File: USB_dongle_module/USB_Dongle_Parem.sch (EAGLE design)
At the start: 29 parts, among them IC3 FT230XS, X1 USB-A

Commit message: Board
Board olemas, veidi vajab veel üle vaatamist, kuid oelemas siiski.
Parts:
- C7: device eagle-ltspice:CC0603 -> eagle-ltspice:CC1206
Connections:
- net TXD: now also R11.1
- net VCCIO: no longer R11.1
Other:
- moved on the sheet: C10, C7, R11, R12

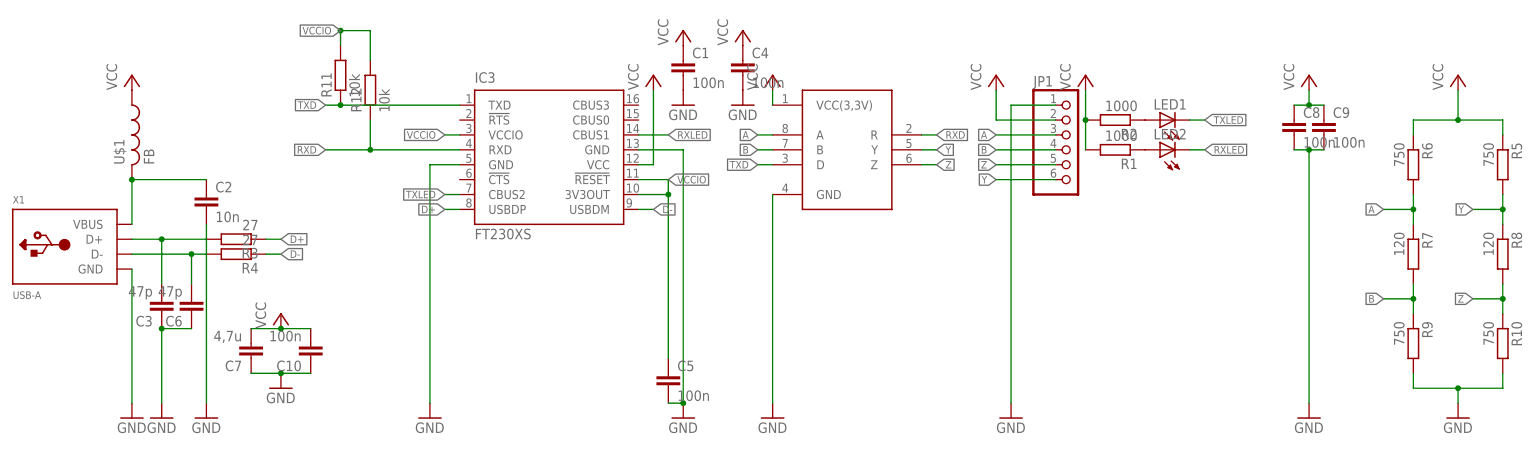
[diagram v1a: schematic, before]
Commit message: Korrastasin boardi
Tegin mõned muudatused skeemis ning korrastasin boardi. Valmis!
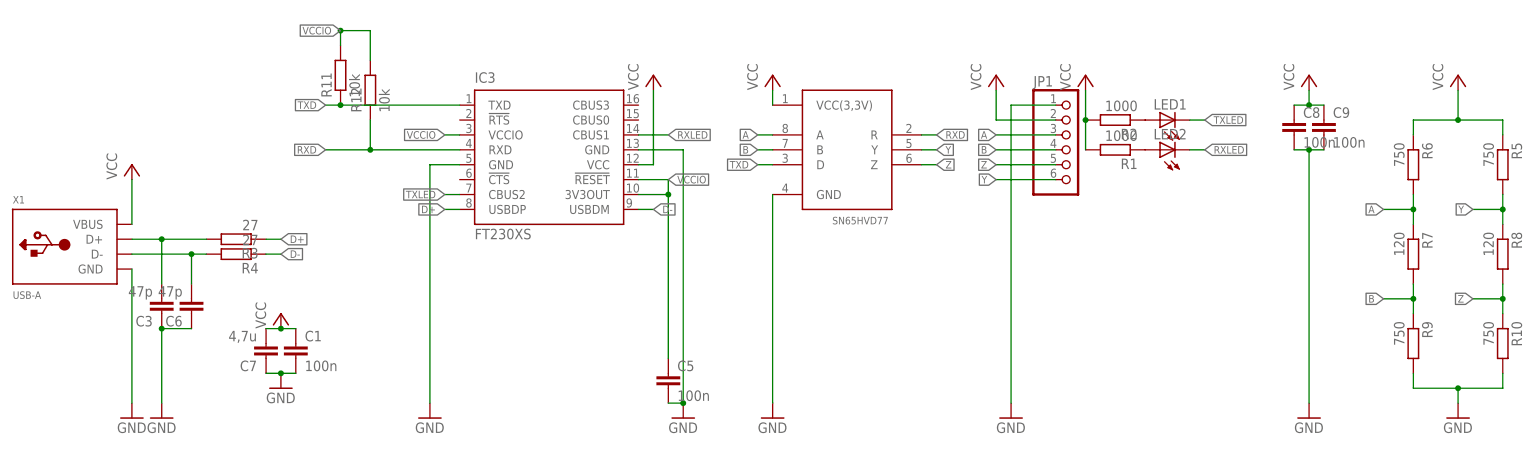
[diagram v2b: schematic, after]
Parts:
- removed C10, C4: 100n, eagle-ltspice:CC0603
- removed C2: 10n, eagle-ltspice:CC0603
- removed U$1: FB, adafruit:FB
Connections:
- removed net N$6: C2.1, U$1.2, X1.VBUS
- net GND: no longer C10.1, C2.2, C4.2
- net VCC: now also X1.VBUS; no longer C10.2, C4.1, U$1.1
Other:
- moved on the sheet: C1, C7

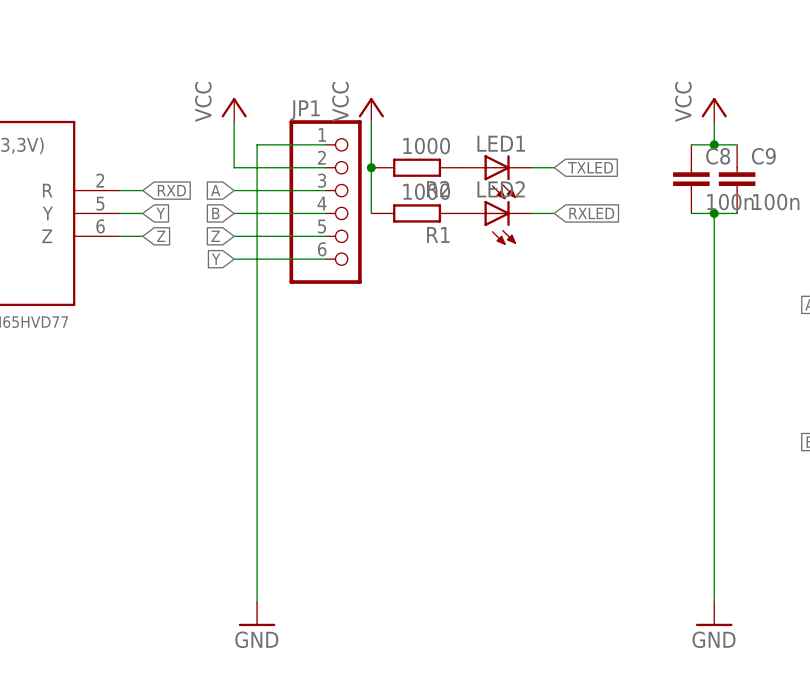
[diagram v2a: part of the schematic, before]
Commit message: Pinheader>Micromatch
Vahetasin siis komponendi välja, lisaks muutsin kondekate asukohta.
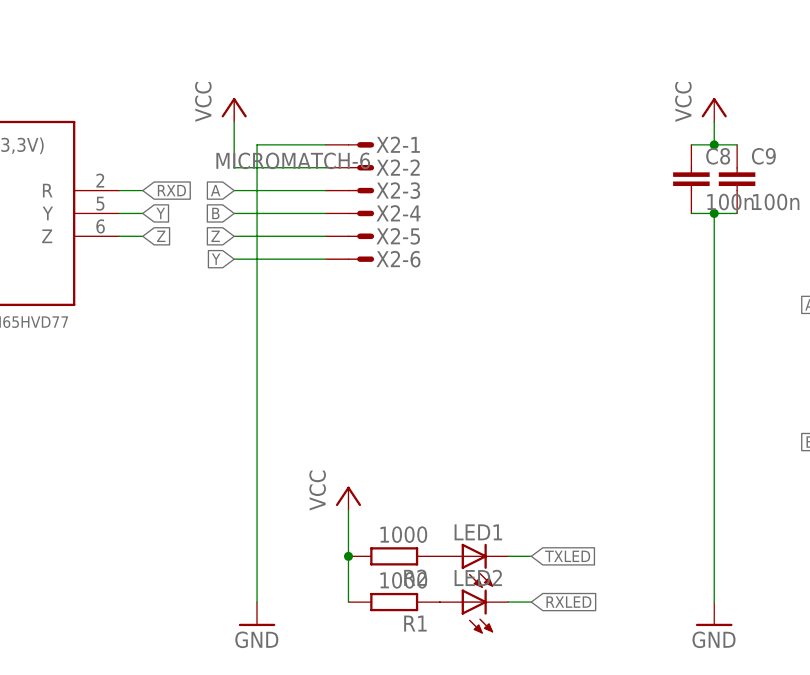
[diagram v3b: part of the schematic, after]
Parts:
- removed JP1: (no value), pinhead:PINHD-1X6
- added X2: MICROMATCH-6, con-amp-micromatch:MICROMATCH-6
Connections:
- net A: now also X2-3.S; no longer JP1.3
- net B: now also X2-4.S; no longer JP1.4
- net GND: now also X2-1.S; no longer JP1.1
- net VCC: now also X2-2.S; no longer JP1.2
- net Y: now also X2-6.S; no longer JP1.6
- net Z: now also X2-5.S; no longer JP1.5
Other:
- moved on the sheet: LED1, LED2, R1, R2
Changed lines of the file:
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@@
 <part name="P+4" library="supply1" deviceset="VCC" device=""/>
 <part name="GND5" library="supply1" deviceset="GND" device=""/>
-<part name="JP1" library="pinhead" deviceset="PINHD-1X6" device=""/>
 <part name="GND6" library="supply1" deviceset="GND" device=""/>
 <part name="P+8" library="supply1" deviceset="VCC" device=""/>
@@
 <part name="R11" library="resistor" deviceset="R-EU_" device="R0603" value="10k"/>
 <part name="R12" library="resistor" deviceset="R-EU_" device="R0603" value="10k"/>
+<part name="X2" library="con-amp-micromatch" deviceset="MICROMATCH-6" device=""/>
 </parts>
 <sheets>
@@
 <instance part="GND1" gate="1" x="15.24" y="53.34"/>
 <instance part="P+1" gate="VCC" x="15.24" y="96.52"/>
-<instance part="LED1" gate="G$1" x="190.5" y="104.14" rot="R90"/>
-<instance part="LED2" gate="G$1" x="190.5" y="99.06" rot="R90"/>
-<instance part="R1" gate="G$1" x="182.88" y="99.06" rot="R180"/>
-<instance part="R2" gate="G$1" x="182.88" y="104.14" rot="R180"/>
-<instance part="P+3" gate="VCC" x="177.8" y="111.76"/>
+<instance part="LED1" gate="G$1" x="187.96" y="60.96" rot="R90"/>
+<instance part="LED2" gate="G$1" x="187.96" y="55.88" rot="R90"/>
+<instance part="R1" gate="G$1" x="180.34" y="55.88" rot="R180"/>
+<instance part="R2" gate="G$1" x="180.34" y="60.96" rot="R180"/>
+<instance part="P+3" gate="VCC" x="175.26" y="68.58"/>
 <instance part="U$2" gate="G$1" x="134.62" y="96.52"/>
 <instance part="GND9" gate="1" x="124.46" y="53.34"/>
@@
 <instance part="P+4" gate="VCC" x="215.9" y="111.76"/>
 <instance part="GND5" gate="1" x="215.9" y="53.34"/>
-<instance part="JP1" gate="A" x="175.26" y="99.06"/>
 <instance part="GND6" gate="1" x="165.1" y="53.34"/>
 <instance part="P+8" gate="VCC" x="162.56" y="111.76"/>
@@
 <instance part="R11" gate="G$1" x="50.8" y="111.76" rot="R90"/>
 <instance part="R12" gate="G$1" x="55.88" y="109.22" rot="R90"/>
+<instance part="X2" gate="-1" x="177.8" y="106.68" rot="R180"/>
+<instance part="X2" gate="-2" x="177.8" y="104.14" rot="R180"/>
+<instance part="X2" gate="-3" x="177.8" y="101.6" rot="R180"/>
+<instance part="X2" gate="-4" x="177.8" y="99.06" rot="R180"/>
+<instance part="X2" gate="-5" x="177.8" y="96.52" rot="R180"/>
+<instance part="X2" gate="-6" x="177.8" y="93.98" rot="R180"/>
 </instances>
 <busses>
@@
 </segment>
 <segment>
-<pinref part="JP1" gate="A" pin="1"/>
 <wire x1="165.1" y1="106.68" x2="172.72" y2="106.68" width="0.1524" layer="91"/>
 <wire x1="165.1" y1="106.68" x2="165.1" y2="55.88" width="0.1524" layer="91"/>
 <pinref part="GND6" gate="1" pin="GND"/>
+<pinref part="X2" gate="-1" pin="S"/>
 </segment>
 <segment>
@@
 <pinref part="P+3" gate="VCC" pin="VCC"/>
 <pinref part="R2" gate="G$1" pin="2"/>
-<wire x1="177.8" y1="109.22" x2="177.8" y2="104.14" width="0.1524" layer="91"/>
+<wire x1="175.26" y1="66.04" x2="175.26" y2="60.96" width="0.1524" layer="91"/>
 <pinref part="R1" gate="G$1" pin="2"/>
-<wire x1="177.8" y1="99.06" x2="177.8" y2="104.14" width="0.1524" layer="91"/>
-<junction x="177.8" y="104.14"/>
+<wire x1="175.26" y1="55.88" x2="175.26" y2="60.96" width="0.1524" layer="91"/>
+<junction x="175.26" y="60.96"/>
 </segment>
 <segment>
@@
 <segment>
 <wire x1="172.72" y1="104.14" x2="162.56" y2="104.14" width="0.1524" layer="91"/>
-<pinref part="JP1" gate="A" pin="2"/>
 <wire x1="162.56" y1="104.14" x2="162.56" y2="109.22" width="0.1524" layer="91"/>
 <pinref part="P+8" gate="VCC" pin="VCC"/>
+<pinref part="X2" gate="-2" pin="S"/>
 </segment>
 <segment>
@@
 <segment>
 <pinref part="LED2" gate="G$1" pin="C"/>
-<wire x1="195.58" y1="99.06" x2="198.12" y2="99.06" width="0.1524" layer="91"/>
-<label x="198.12" y="99.06" size="1.27" layer="95" xref="yes"/>
+<wire x1="193.04" y1="55.88" x2="195.58" y2="55.88" width="0.1524" layer="91"/>
+<label x="195.58" y="55.88" size="1.27" layer="95" xref="yes"/>
 </segment>
 <segment>
@@
 <segment>
 <pinref part="LED1" gate="G$1" pin="C"/>
-<wire x1="195.58" y1="104.14" x2="198.12" y2="104.14" width="0.1524" layer="91"/>
-<label x="198.12" y="104.14" size="1.27" layer="95" xref="yes"/>
+<wire x1="193.04" y1="60.96" x2="195.58" y2="60.96" width="0.1524" layer="91"/>
+<label x="195.58" y="60.96" size="1.27" layer="95" xref="yes"/>
 </segment>
 <segment>
@@
 <label x="162.56" y="99.06" size="1.27" layer="95" rot="R180" xref="yes"/>
 <wire x1="172.72" y1="99.06" x2="162.56" y2="99.06" width="0.1524" layer="91"/>
-<pinref part="JP1" gate="A" pin="4"/>
+<pinref part="X2" gate="-4" pin="S"/>
 </segment>
 <segment>
@@
 <segment>
 <wire x1="172.72" y1="93.98" x2="162.56" y2="93.98" width="0.1524" layer="91"/>
-<pinref part="JP1" gate="A" pin="6"/>
 <label x="162.56" y="93.98" size="1.27" layer="95" rot="R180" xref="yes"/>
+<pinref part="X2" gate="-6" pin="S"/>
 </segment>
 <segment>
@@
 <segment>
 <wire x1="172.72" y1="96.52" x2="162.56" y2="96.52" width="0.1524" layer="91"/>
-<pinref part="JP1" gate="A" pin="5"/>
 <label x="162.56" y="96.52" size="1.27" layer="95" rot="R180" xref="yes"/>
+<pinref part="X2" gate="-5" pin="S"/>
 </segment>
 <segment>
@@
 <label x="162.56" y="101.6" size="1.27" layer="95" rot="R180" xref="yes"/>
 <wire x1="172.72" y1="101.6" x2="162.56" y2="101.6" width="0.1524" layer="91"/>
-<pinref part="JP1" gate="A" pin="3"/>
+<pinref part="X2" gate="-3" pin="S"/>
 </segment>
 <segment>
@@
 </sheet>
 </sheets>
+<errors>
+</errors>
 </schematic>
 </drawing>
